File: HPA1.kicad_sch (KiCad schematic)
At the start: 96 parts, among them J1 Power, J2 Input, J3 Output, J4 Mute, J5 Conn_01x01_Male, K1 G6H-2, Q1 BC560C, Q10 BC549C, Q11 BC549C, Q12 TTA004B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

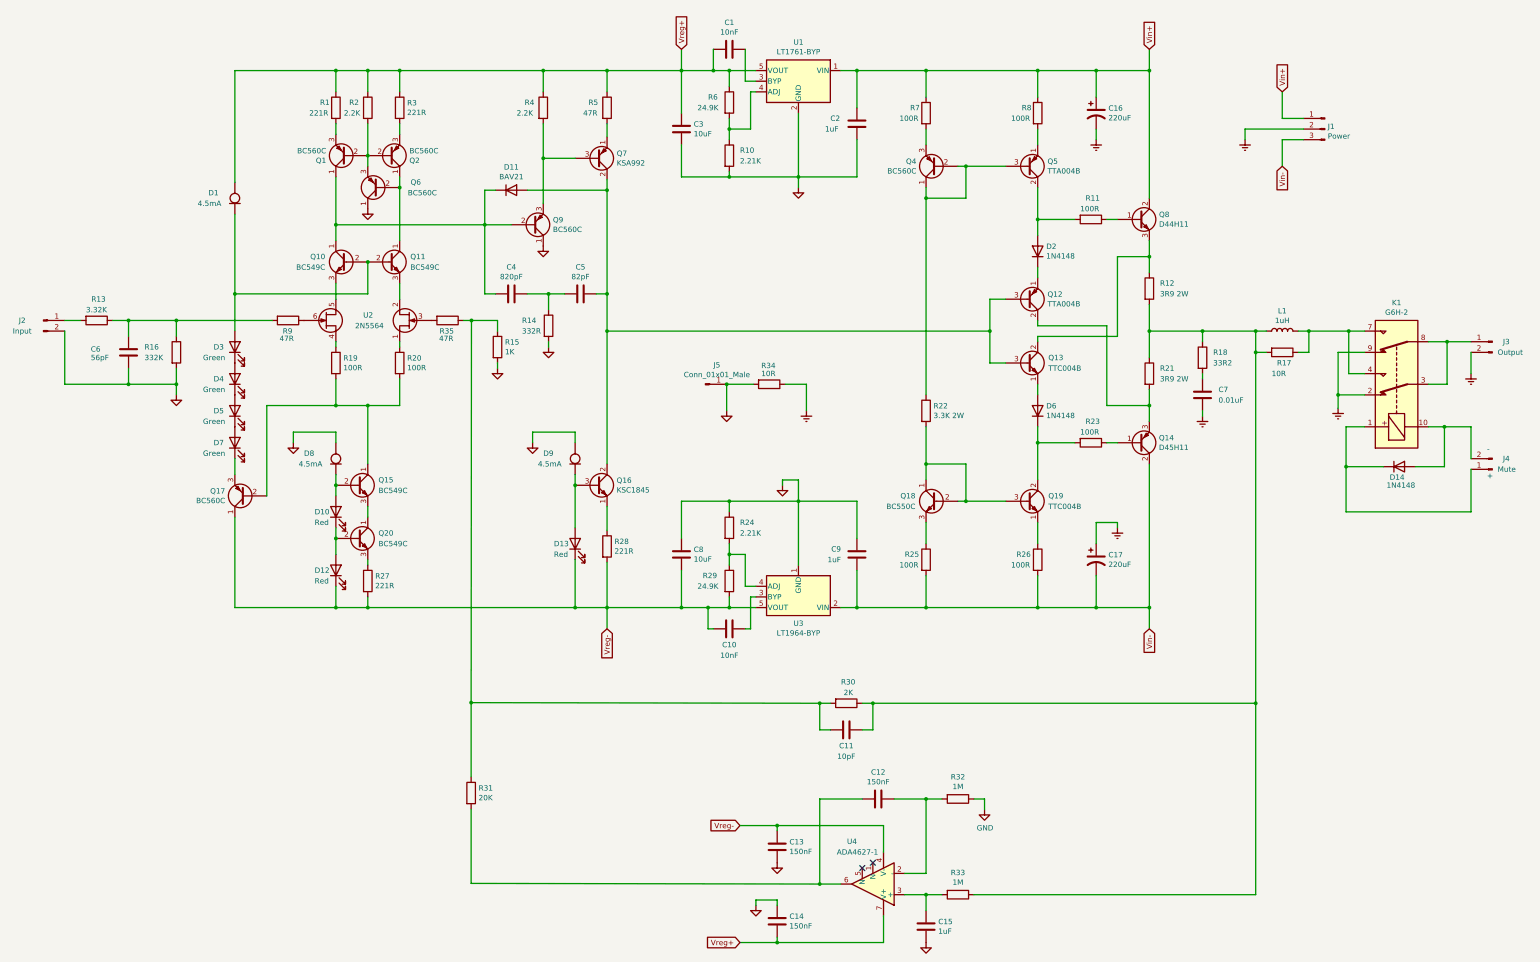
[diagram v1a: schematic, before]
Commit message: Created local symbol and footprint libraries. Updated schematic and PCB. Fixed all rule check errors.
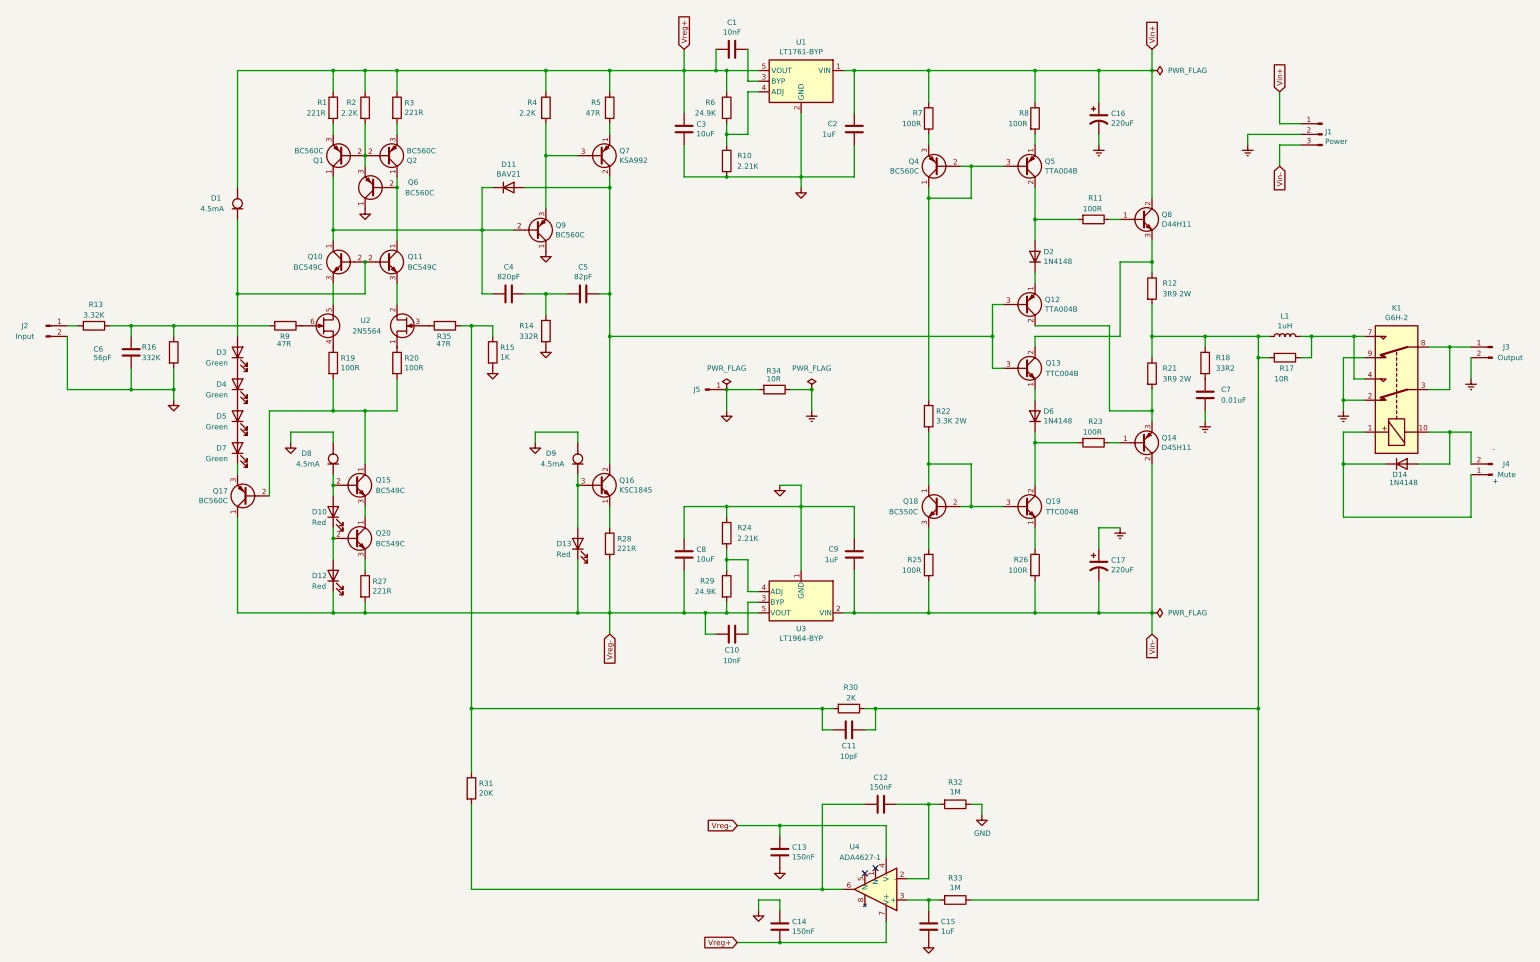
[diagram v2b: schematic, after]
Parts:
- C1, C10: footprint Capacitor_SMD:C_0805_2012Metric_Pad1.15x1.40mm_HandSolder -> Capacitor_SMD:C_0805_2012Metric_Pad1.18x1.45mm_HandSolder
- C16, C17: symbol HPA1-rescue:CP1-Device -> Device:C_Polarized_US
- D1, D8, D9: footprint Diode_THT:D_DO-35_SOD27_P7.62mm_Horizontal -> HPA1-footprints:D_DO-35_SOD27_P7.62mm_Horizontal; symbol HPA1-rescue:CRD-HP_Miscellaneous -> HPA1_symbols:CRD
- D11, D14, D2, D6: footprint Diode_THT:D_DO-35_SOD27_P7.62mm_Horizontal -> HPA1-footprints:D_DO-35_SOD27_P7.62mm_Horizontal
- J1: footprint HP_Footprints:3-pad-wire-connector-22-ga -> HPA1-footprints:3-pad-wire-connector-22-ga; symbol HPA1-rescue:Conn_01x03_Male-Connector -> Connector:Conn_01x03_Pin
- J2, J3: footprint HP_Footprints:2-pad-wire-connector-small -> HPA1-footprints:2-pad-wire-connector-22-ga; symbol HPA1-rescue:Conn_01x02_Male-Connector -> Connector:Conn_01x02_Pin
- J4: footprint HP_Footprints:2-pad-wire-connector-22-ga -> HPA1-footprints:2-pad-wire-connector-22-ga; symbol HPA1-rescue:Conn_01x02_Male-Connector -> Connector:Conn_01x02_Pin
- J5: footprint HP_Footprints:1-pad-wire-connector-22-ga -> HPA1-footprints:1-pad-wire-connector-22-ga; symbol HPA1-rescue:Conn_01x01_Male-Connector -> Connector:Conn_01x01_Pin
- L1: footprint HP_Footprints:HPA-Output-Coil -> HPA1-footprints:HPA-Output-Coil
- Q1, Q17, Q2, Q4, Q6, Q9: symbol Transistor_BJT:BC560 -> Transistor_BJT:Q_PNP_CBE
- Q10, Q11, Q15, Q18, Q20: symbol Transistor_BJT:BC550 -> Transistor_BJT:Q_NPN_CBE
- Q14: symbol Device:Q_PNP_BCE -> Transistor_BJT:Q_PNP_BCE
- Q16: symbol Device:Q_NPN_ECB -> Transistor_BJT:Q_NPN_ECB
- Q7: symbol Device:Q_PNP_ECB -> Transistor_BJT:Q_PNP_ECB
- Q8: symbol Device:Q_NPN_BCE -> Transistor_BJT:Q_NPN_BCE
- R10, R24, R29, R32, R33, R6: footprint Resistor_SMD:R_0805_2012Metric_Pad1.15x1.40mm_HandSolder -> HPA1-footprints:R_0805_2012Metric_Pad1.15x1.40mm_HandSolder
- U1, U3: footprint Package_TO_SOT_SMD:TSOT-23-5 -> HPA1-footprints:TSOT-23-5
- U2: footprint HP_Footprints:TO-71-6 -> HPA1-footprints:TO-71-6; symbol HPA1-rescue:2N5564-HP-Transistor_FET -> HPA1_symbols:2N5564
- U4: symbol HPA1-rescue:ADA4627-1-HP_Op_Amps -> HPA1_symbols:ADA4627-1
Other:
- moved on the sheet: C1, C10, C11, C12, C13, C14, C15, C16, C17, C2, C3, C4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
